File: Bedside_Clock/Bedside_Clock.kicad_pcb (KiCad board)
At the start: 2 copper layers, 177.8 x 68.6 mm, 199 parts, among them J1 USBC_USB2.0, SW3 BOOT, SW4 RESET, U1 ESP32-C3-MINI-1

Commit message: [HW] Swap component names from SK9822 to HD107S
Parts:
- D10, D11, D12, D13, D14, D15, D16, D17, D18, D19, D2, D20, D21, D23, D24, D25, D26, D27, D28, D29, D3, D30, D31, D32, D33, D34, D35, D36, D37, D38, D39, D4, D40, D41, D42, D43, D44, D46, D47, D48, D49, D5, D50, D51, D52, D53, D54, D55, D56, D57, D58, D59, D6, D60, D61, D62, D63, D64, D65, D67, D68, D69, D7, D70, D71, D72, D73, D74, D75, D76, D77, D78, D79, D8, D80, D81, D82, D83, D84, D85, D86, D9: value SK9822 -> HD107S

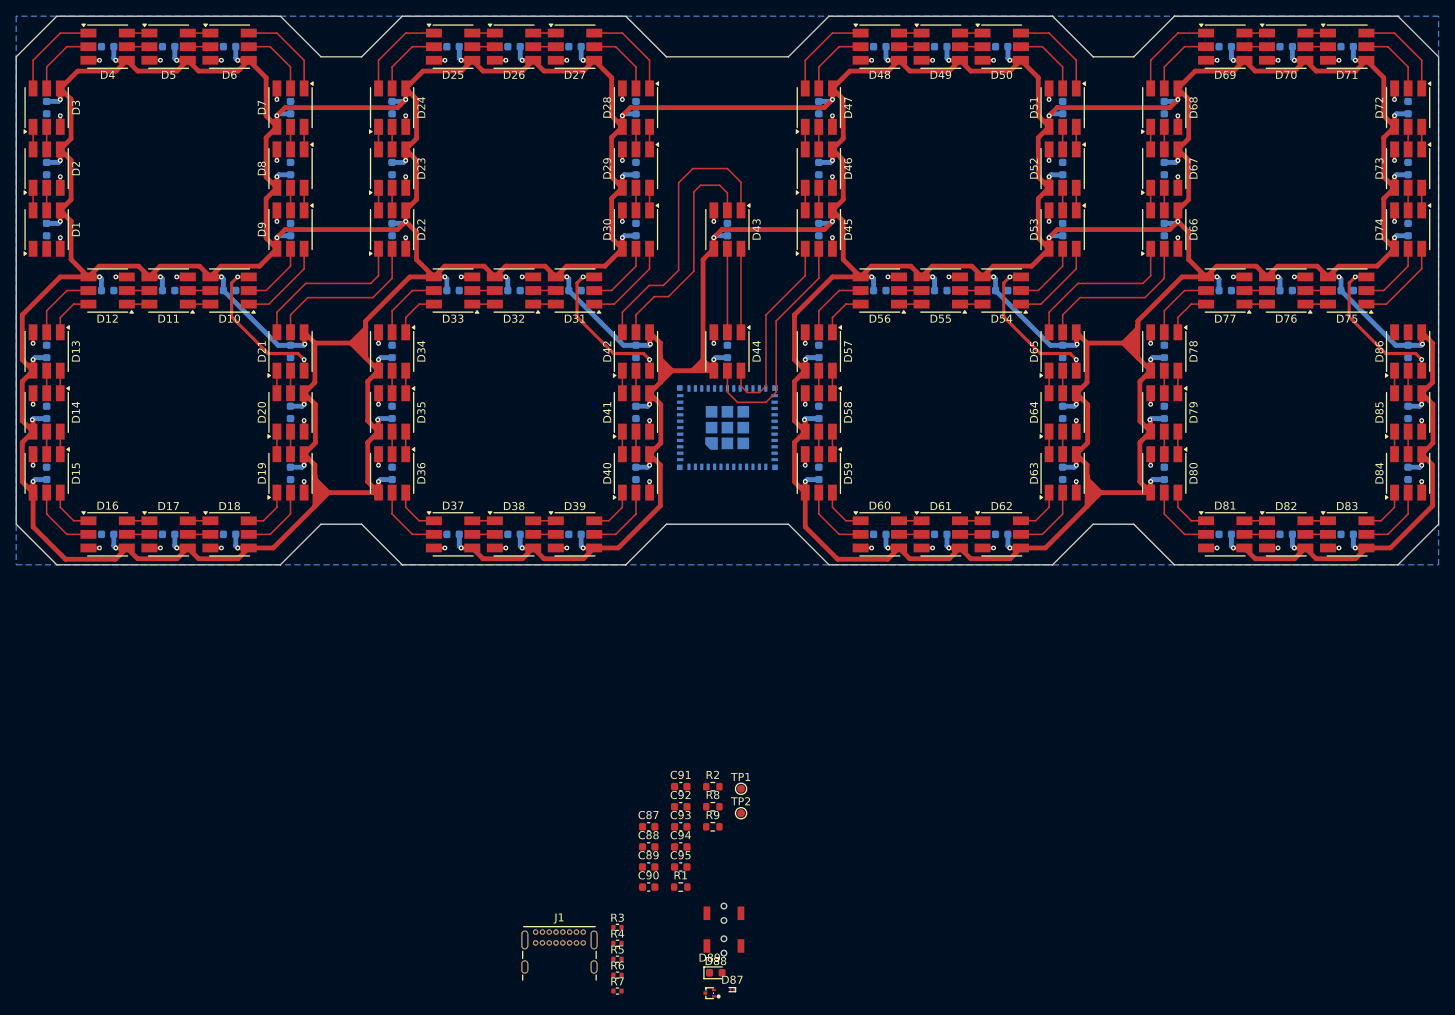
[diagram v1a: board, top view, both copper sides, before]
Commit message: [HW] Routing progress Need to close on some parts
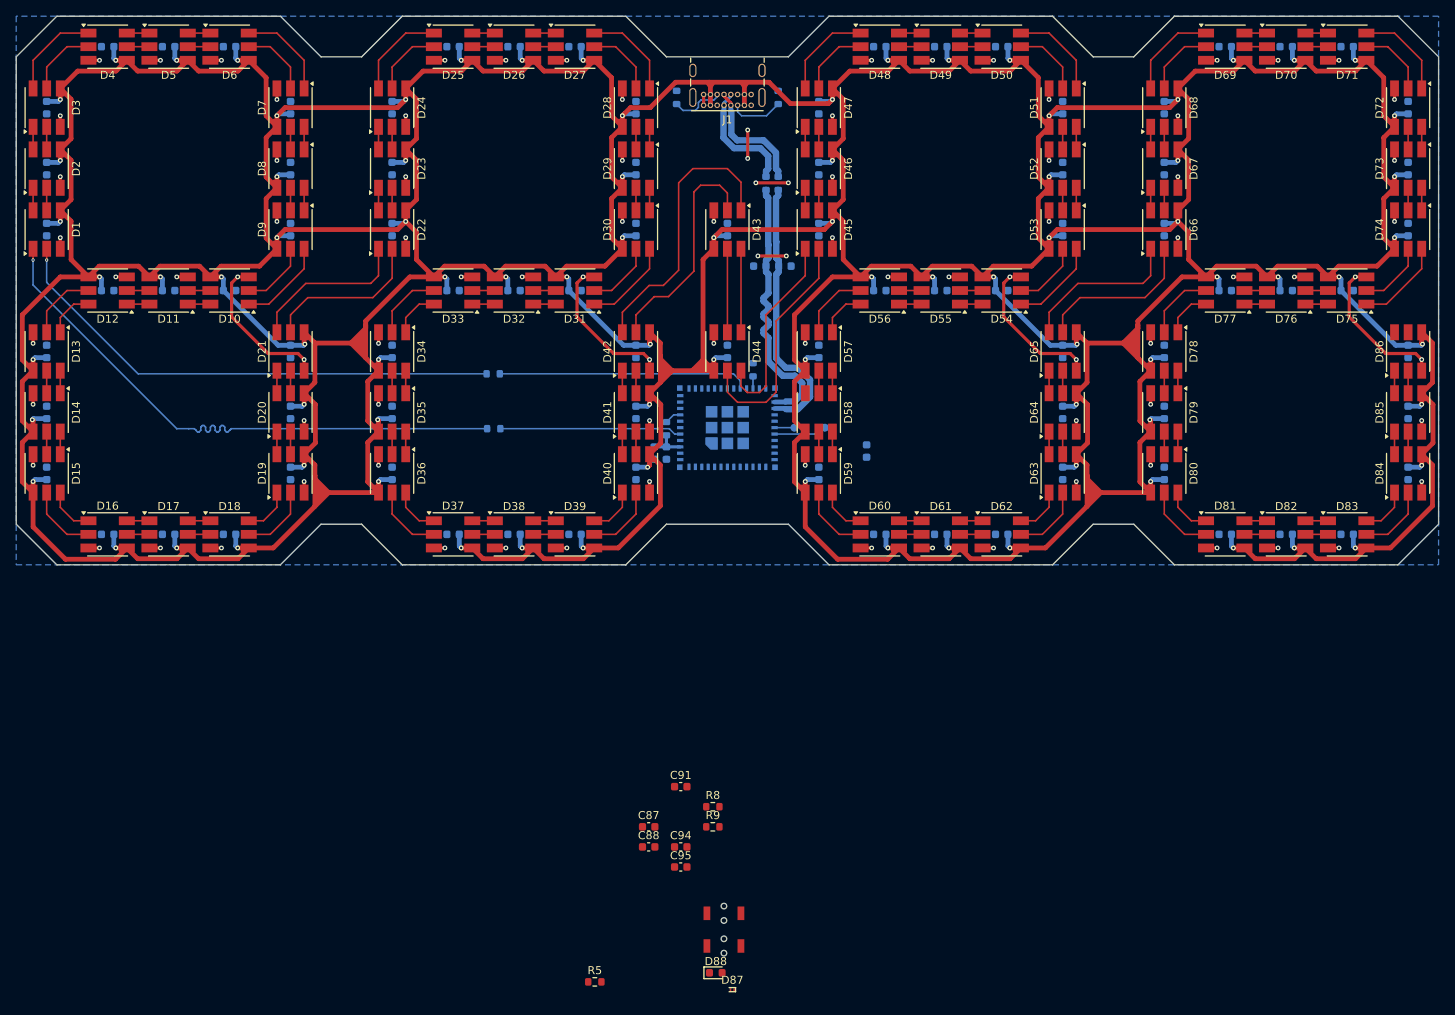
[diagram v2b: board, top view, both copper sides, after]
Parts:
- removed D89: TPD2EUSB30, EasyEDA2KiCad:SOT-723_L1.2-W0.8-P0.80-LS1.2-BR
- added R10: 0, Resistor_SMD:R_0603_1608Metric, B.Cu at (91.4, 88.4)
- added R11: 0, Resistor_SMD:R_0603_1608Metric, B.Cu at (91.4, 81.5)
- C89, C90, C92, C93, R1, R2, TP1, TP2: moved to B.Cu
- R3, R4, R6, R7: footprint Resistor_SMD:R_0402_1005Metric -> Resistor_SMD:R_0603_1608Metric; moved to B.Cu
- R5: footprint Resistor_SMD:R_0402_1005Metric -> Resistor_SMD:R_0603_1608Metric
- moved J1 106.8 mm to (123.6, 48.0), turned to 180 degrees
- moved R7 102.7 mm to (125.5, 57.7), turned to 90 degrees
- moved R6 101.0 mm to (127.0, 57.7), turned to 90 degrees
- moved R1 98.7 mm to (114.3, 47.0), turned to -90 degrees
- moved R2 86.5 mm to (127.0, 47.0), turned to -90 degrees
- moved R4 73.7 mm to (123.8, 81.0), turned to 90 degrees
- moved C93 70.8 mm to (124.7, 68.1)
- moved C92 68.8 mm to (127.8, 68.1), turned to 180 degrees
- moved R3 62.6 mm to (113.0, 88.4), turned to 90 degrees
- moved C90 54.3 mm to (113.0, 91.4), turned to -90 degrees
- moved C89 51.7 mm to (111.5, 91.4), turned to -90 degrees
- moved TP2 48.7 mm to (129.0, 88.3), turned to 90 degrees
- moved TP1 46.3 mm to (132.8, 88.3), turned to -90 degrees
- moved C58 7.68 mm to (138.0, 91.2)
- moved R5 4.01 mm to (104.1, 157.5)
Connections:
- net /USB_D'+ renamed /UD'+
- net /USB_D'- renamed /UD'-
- D1 pad 1: DO -> /Digit0/DI
- D1 pad 2: CO -> /Digit0/CI
- J1 pad A6: UD+ -> /UD+
- J1 pad A7: UD- -> /UD-
- J1 pad B6: UD+ -> /UD+
- J1 pad B7: UD- -> /UD-
- R6 pad 2: USB_D+ -> /UD+
- R7 pad 2: USB_D- -> /UD-
- U1 pad 20: CO -> /CO
- U1 pad 5: DO -> /DO
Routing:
- net /Digit0/DI: track 0.00 -> 72.5 mm, vias 0 -> 1
- net /Digit0/CI: track 0.00 -> 63.9 mm, vias 0 -> 1
- net /UD'+: track 0.00 -> 34.0 mm
- net /UD'-: track 0.00 -> 33.9 mm
- net /CO: track 0.00 -> 31.4 mm
- net /DO: track 0.00 -> 22.8 mm
- net /UD+: track 0.00 -> 15.0 mm
- net /UD-: track 0.00 -> 15.0 mm
- net GND: track 185.4 -> 196.5 mm, vias 86 -> 91
- net /CC2: track 0.00 -> 6.75 mm
- net /CC1: track 0.00 -> 6.69 mm
- net Net-(U1-GPIO21/U0TXD): track 0.00 -> 6.61 mm
- net +3V3: track 0.00 -> 4.69 mm
- net +5V: track 1321.4 -> 1325.9 mm, vias 86 -> 85
- net Net-(U1-GPIO20/U0RXD): track 0.00 -> 2.48 mm
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
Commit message: [HW] Switch to 4 layers
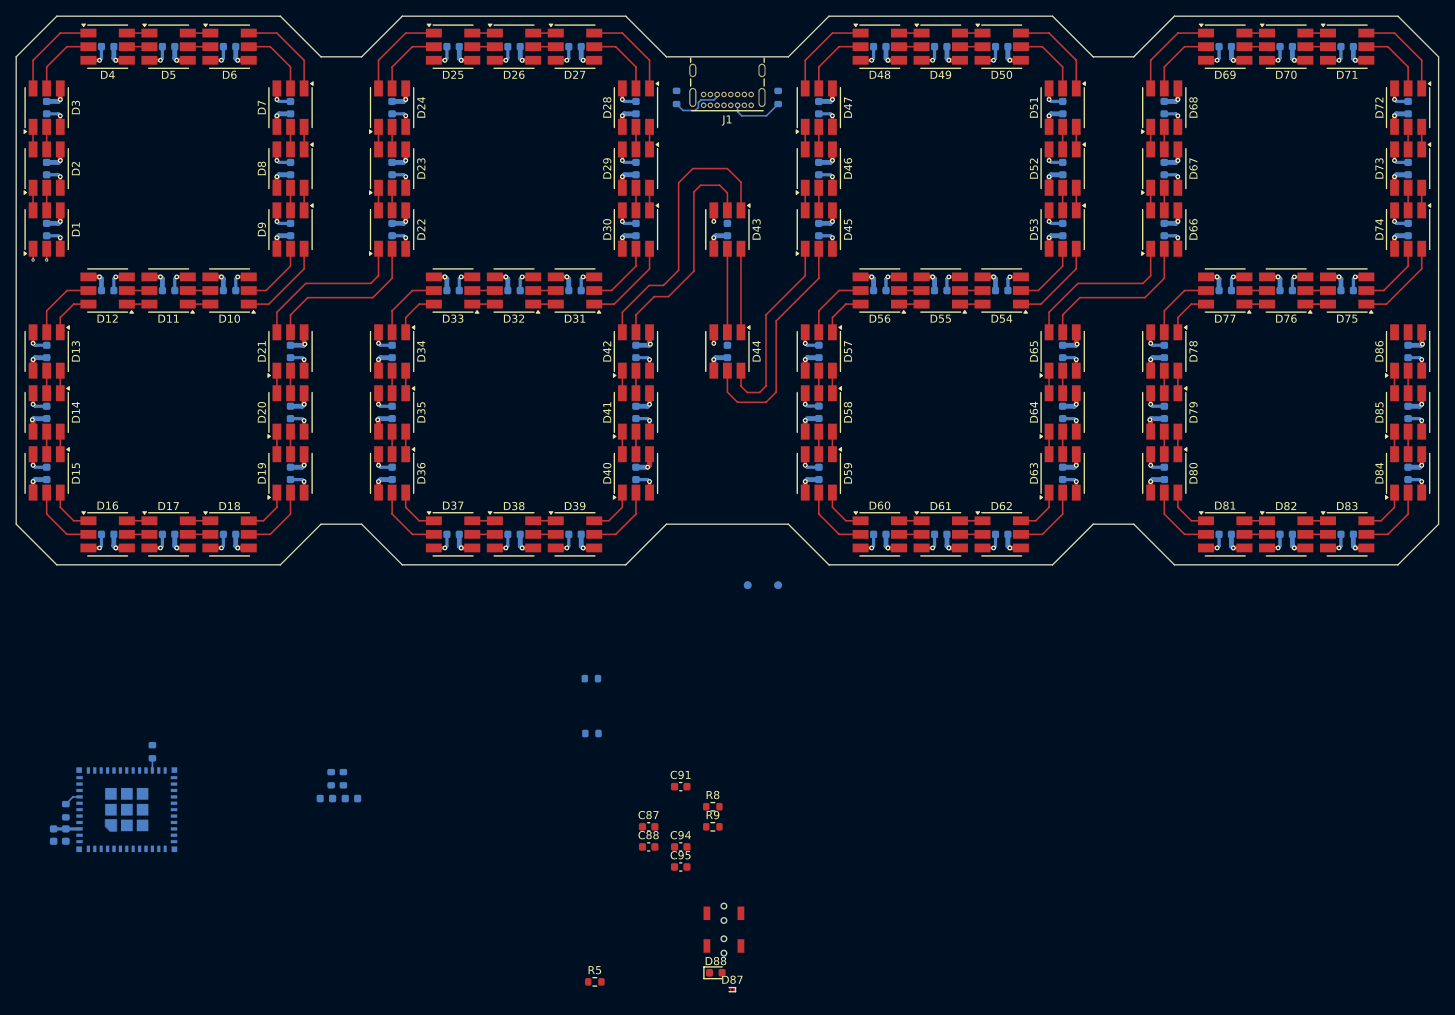
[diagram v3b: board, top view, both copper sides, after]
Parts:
- moved R6 92.2 mm to (72.6, 132.1)
- moved R7 92.2 mm to (71.1, 132.1)
- moved U1 89.0 mm to (45.6, 136.0)
- moved R4 89.0 mm to (48.8, 128.8)
- moved C89 89.0 mm to (36.4, 139.2)
- moved C90 89.0 mm to (38.0, 139.2)
- moved R3 89.0 mm to (38.0, 136.1)
- moved C92 85.8 mm to (73.7, 134.6)
- moved C93 85.8 mm to (70.5, 134.6)
- moved R10 40.0 mm to (103.7, 126.5)
- moved R11 40.0 mm to (103.7, 119.6)
- moved TP2 20.5 mm to (123.2, 108.0)
- moved TP1 20.5 mm to (127.0, 108.0)
- moved C58 7.68 mm to (132.1, 86.3)
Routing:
- net +5V: track 1325.9 -> 274.8 mm, vias 85 -> 86
- net GND: track 196.5 -> 269.9 mm, vias 91 -> 86
- net /Digit0/DI: track 72.5 -> 1.41 mm
- net /Digit0/CI: track 63.9 -> 1.41 mm
- net /UD'+: track 34.0 -> 0.00 mm
- net /UD'-: track 33.9 -> 0.00 mm
- net /CO: track 31.4 -> 0.00 mm
- net /DO: track 22.8 -> 0.00 mm
- net /UD+: track 15.0 -> 0.00 mm
- net /UD-: track 15.0 -> 0.00 mm
- net Net-(U1-GPIO21/U0TXD): track 6.61 -> 0.00 mm
- net Net-(U1-GPIO20/U0RXD): track 2.48 -> 0.00 mm
- net +3V3: track 4.69 -> 3.24 mm
- added copper zone on In1.Cu, net +5V
- added copper zone on In2.Cu, net GND
- removed copper zone on B.Cu, net GND
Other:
- copper layers 2 -> 4

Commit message: [HW] Switch to 4 layers and m mid mount USB-C
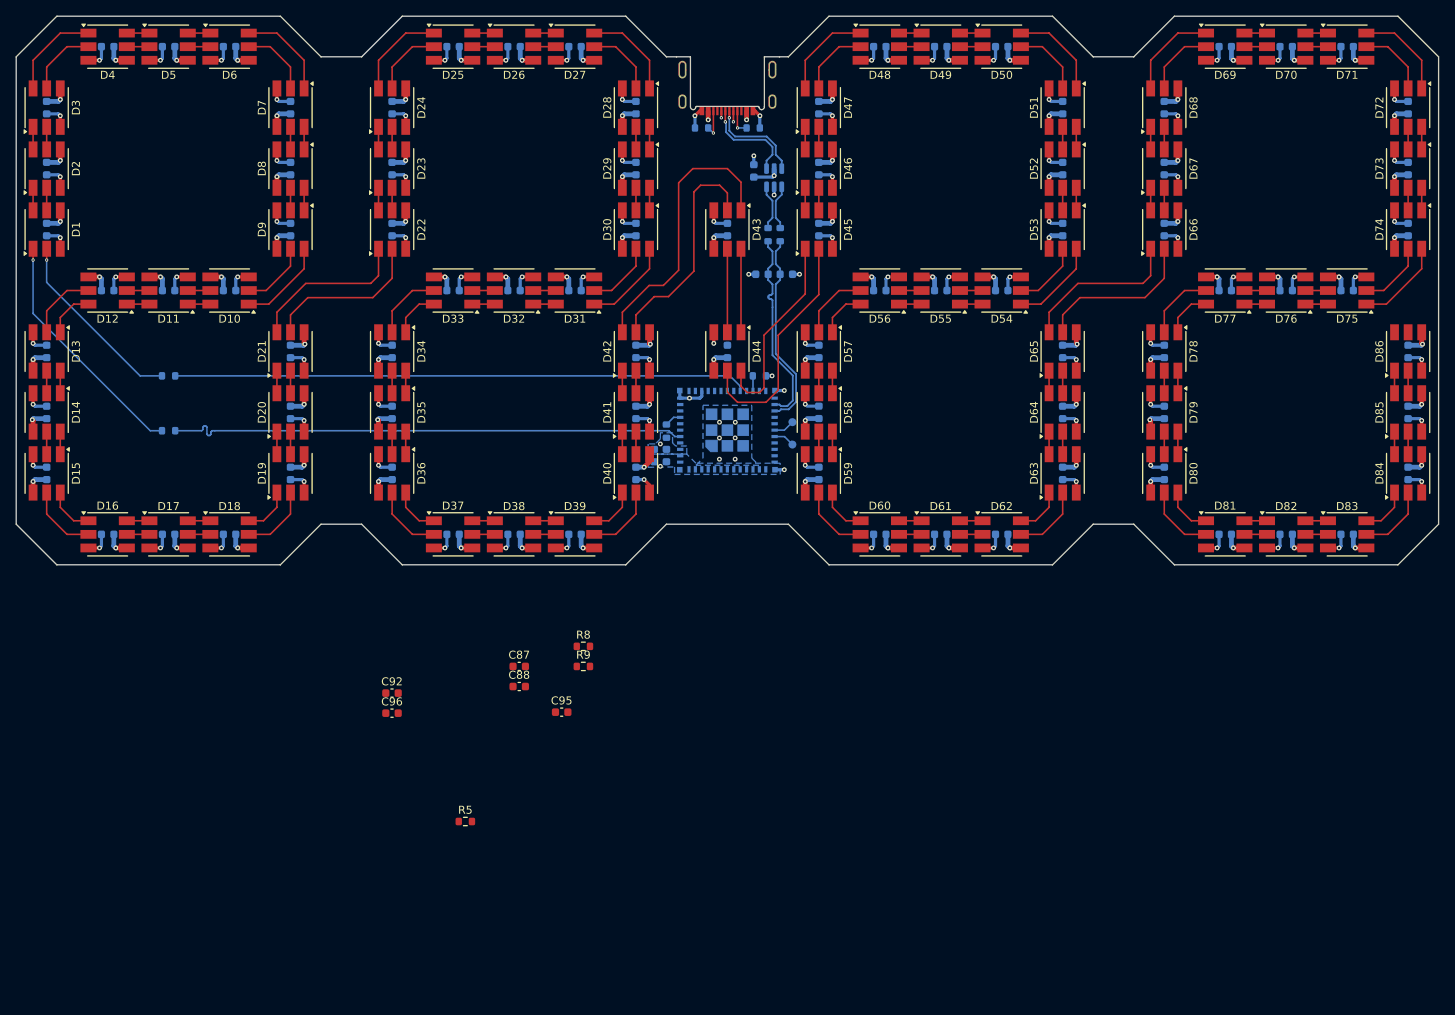
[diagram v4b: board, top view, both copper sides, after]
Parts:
- removed the C91 at (114.8, 133.1)
- removed the C94 at (114.8, 140.7)
- removed D87: TVS, EasyEDA2KiCad:X2SON-2_L0.6-W0.3-P0.35_ESD441DPLR
- removed D88: GREEN, LED_SMD:LED_0603_1608Metric
- removed SW3: BOOT, EasyEDA2KiCad:KEY-SMD_L3.9-W3.0-LS5.0-EH
- removed SW4: RESET, EasyEDA2KiCad:KEY-SMD_L3.9-W3.0-LS5.0-EH
- added C89: 100nF, Capacitor_SMD:C_0603_1608Metric, B.Cu at (124.0, 56.2)
- added C92: 1uF, Capacitor_SMD:C_0603_1608Metric, F.Cu at (78.7, 121.4)
- added C96: 100nF, Capacitor_SMD:C_0603_1608Metric, F.Cu at (78.7, 124.0)
- added U2: USBLC6-2SC6, Package_TO_SOT_SMD:SOT-23-6, B.Cu at (126.5, 57.0)
- C90: value 100nF -> 10uF
- C91: renamed from C89; value 10uF -> 100nF
- J1: footprint Connector_USB:USB_C_Receptacle_GCT_USB4085 -> USB4520_03_0_A:GCT_USB4520-03-0-A_REVA
- moved R4 89.2 mm to (124.7, 81.8), turned to 0 degrees
- moved U1 88.8 mm to (120.7, 88.6)
- moved C90 88.8 mm to (113.0, 91.7)
- moved C91 88.8 mm to (111.5, 91.7)
- moved R3 88.8 mm to (113.0, 88.7)
- moved R6 87.2 mm to (127.3, 64.1)
- moved R7 87.2 mm to (125.7, 64.1)
- moved C94 85.2 mm to (125.0, 69.1), turned to 180 degrees
- moved C93 85.1 mm to (128.0, 69.1), turned to 0 degrees
- moved R10 65.1 mm to (50.8, 88.6)
- moved R11 65.0 mm to (50.8, 81.8)
- moved C87 25.8 mm to (94.6, 118.1)
- moved R9 25.8 mm to (102.6, 118.1)
- moved C88 25.8 mm to (94.6, 120.6)
- moved R8 25.8 mm to (102.6, 115.6)
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- renumbered C92 to C93, C93 to C94
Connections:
- net COLOR renamed /COLOR
- net MODE renamed /MODE
- C93 pad 1: GND -> /UD'+
- C93 pad 2: /UD'+ -> GND
- C94 pad 1: GND -> /UD'-
- C94 pad 2: /UD'- -> GND
- C95 pad 1: CHIP_EN -> /BOOT
- J1 pad A6: /UD+ -> /UD''+
- J1 pad A7: /UD- -> /UD''-
- J1 pad B6: /UD+ -> /UD''+
- J1 pad B7: /UD- -> /UD''-
- J1 pad S1: unconnected-(J1-SHIELD-PadS1) -> GND
- J1 pad S2: unconnected-(J1-SHIELD-PadS2) -> GND
- J1 pad S3: unconnected-(J1-SHIELD-PadS3) -> GND
- J1 pad S4: unconnected-(J1-SHIELD-PadS4) -> GND
- R3 pad 2: CHIP_EN -> /CHIP_EN
- U1 pad 23: BOOT -> /BOOT
- U1 pad 8: CHIP_EN -> /CHIP_EN
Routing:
- net /CO: track 0.00 -> 71.8 mm
- net /DO: track 0.00 -> 65.3 mm
- net /Digit0/DI: track 1.41 -> 30.3 mm
- net /UD'-: track 0.00 -> 25.0 mm
- net /UD'+: track 0.00 -> 25.0 mm
- net /Digit0/CI: track 1.41 -> 23.5 mm
- net GND: track 269.9 -> 287.5 mm, vias 86 -> 102
- net /UD''-: track 0.00 -> 14.7 mm, vias 0 -> 2
- net /UD''+: track 0.00 -> 14.1 mm, vias 0 -> 2
- net /UD+: track 0.00 -> 5.70 mm
- net /UD-: track 0.00 -> 5.70 mm
- net +5V: track 274.8 -> 280.0 mm, vias 86 -> 89
- net /CC1: track 6.69 -> 3.29 mm, vias 0 -> 1
- net /CC2: track 6.75 -> 3.69 mm, vias 0 -> 1
- net Net-(U1-GPIO21/U0TXD): track 0.00 -> 2.64 mm
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- added copper zone on B.Cu, net +3V3
- added copper zone on In1.Cu, net +3V3
- added copper zone on B.Cu, net GND
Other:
- outline, holes or cut-outs redrawn

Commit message: [HW] Clean up and layout improvements
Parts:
- C87, C88, C92, R5, R8, R9: moved to B.Cu
- R1, R2: moved to F.Cu
- moved C88 75.7 mm to (123.9, 50.8)
- moved C87 71.1 mm to (117.4, 50.8), turned to 180 degrees
- moved R5 63.1 mm to (116.7, 81.3), turned to -90 degrees
- moved C92 49.6 mm to (113.0, 85.6), turned to 90 degrees
- moved R9 43.8 mm to (124.7, 80.3)
- moved C96 39.3 mm to (116.1, 111.9)
- moved R8 37.7 mm to (118.2, 81.3), turned to 90 degrees
- moved C95 27.5 mm to (124.1, 110.7)
- moved R11 0.51 mm to (50.8, 81.3)
- moved C44 0.13 mm to (120.5, 78.7)
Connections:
- net /CC1 renamed Net-(J1-CC1)
- net /CC2 renamed Net-(J1-CC2)
- U1 pad 18: unconnected-(U1-GPIO4/ADC1_CH4-Pad18) -> /COLOR
- U1 pad 21: unconnected-(U1-GPIO7-Pad21) -> /MODE
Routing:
- net GND: track 287.5 -> 299.4 mm, vias 102 -> 103
- net /COLOR: track 0.00 -> 4.41 mm, vias 0 -> 1
- net /MODE: track 0.00 -> 4.03 mm, vias 0 -> 1
- net +5V: track 280.0 -> 281.8 mm
- net /LED_BUILTIN: track 0.00 -> 1.57 mm
- net Net-(J1-CC2): track 3.69 -> 2.41 mm, vias 1 -> 0
- net /CHIP_EN: track 2.09 -> 3.24 mm, vias 0 -> 1
- net Net-(J1-CC1): track 3.29 -> 3.06 mm, vias 1 -> 0
